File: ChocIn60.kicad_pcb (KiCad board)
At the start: 2 copper layers, 285 x 94.6 mm, 9 parts

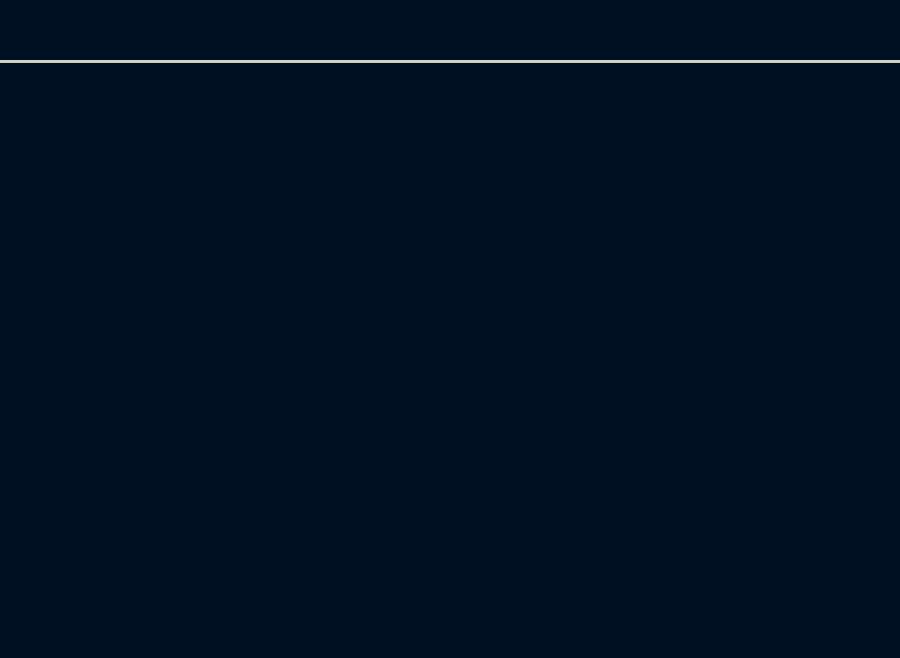
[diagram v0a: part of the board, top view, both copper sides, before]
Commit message: add USB2.0 Type-C Plug.
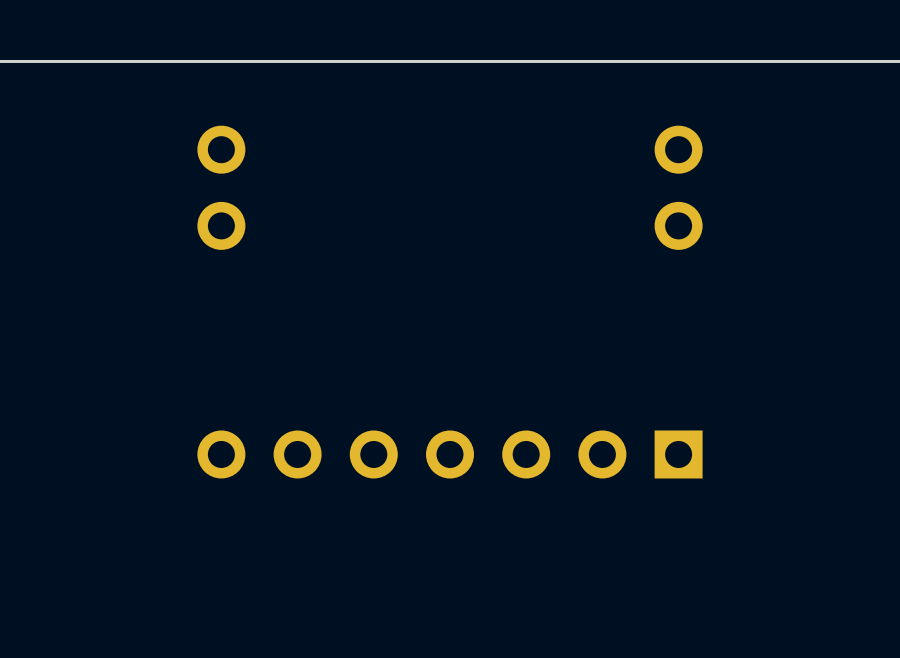
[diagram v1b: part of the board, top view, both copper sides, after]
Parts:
- added P1: USB_C_Plug_USB2.0, Akizuki:AE-USB2.0-TYPE-C, B.Cu at (58.0, 60.0)
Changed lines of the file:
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@@
     (tracks 0)
     (zones 0)
-    (modules 9)
-    (nets 2)
+    (modules 10)
+    (nets 8)
   )
   (page A3)
@@
   (net 0 "")
   (net 1 GND)
+  (net 2 "Net-(P1-PadB5)")
+  (net 3 "Net-(P1-PadA5)")
+  (net 4 "Net-(P1-PadA6)")
+  (net 5 "Net-(P1-PadA7)")
+  (net 6 VCC)
+  (net 7 "Net-(P1-PadS1)")
   (net_class Default "これはデフォルトのネット クラスです。"
     (clearance 0.2)
@@
     (uvia_drill 0.1)
     (add_net GND)
+    (add_net "Net-(P1-PadA5)")
+    (add_net "Net-(P1-PadA6)")
+    (add_net "Net-(P1-PadA7)")
+    (add_net "Net-(P1-PadB5)")
+    (add_net "Net-(P1-PadS1)")
+    (add_net VCC)
+  )
+  (module Akizuki:AE-USB2.0-TYPE-C (layer B.Cu)
+    (at 58 60 180)
+    (descr http://akizukidenshi.com/catalog/g/gK-13080/)
+    (fp_text reference P1 (at 0 -6 180) (layer B.SilkS)
+      (effects (font (size 1 1) (thickness 0.15)) (justify mirror))
+    )
+    (fp_text value USB_C_Plug_USB2.0 (at 0 11 180) (layer B.Fab)
+      (effects (font (size 1 1) (thickness 0.15)) (justify mirror))
+    )
+    (fp_text user GND (at 7.62 0 270 unlocked) (layer B.SilkS)
+      (effects (font (size 1 1) (thickness 0.15)) (justify mirror))
+    )
+    (fp_text user CC2 (at 5.08 0 270 unlocked) (layer B.SilkS)
+      (effects (font (size 1 1) (thickness 0.15)) (justify mirror))
+    )
+    (fp_text user CC1 (at 2.54 0 270 unlocked) (layer B.SilkS)
+      (effects (font (size 1 1) (thickness 0.15)) (justify mirror))
+    )
+    (fp_text user GND (at 0 0 270 unlocked) (layer B.SilkS)
+      (effects (font (size 1 1) (thickness 0.15)) (justify mirror))
+    )
+    (fp_text user D+ (at -2.54 0 270 unlocked) (layer B.SilkS)
+      (effects (font (size 1 1) (thickness 0.15)) (justify mirror))
+    )
+    (fp_text user D- (at -5.08 0 270 unlocked) (layer B.SilkS)
+      (effects (font (size 1 1) (thickness 0.15)) (justify mirror))
+    )
+    (fp_text user VBUS (at -7.62 0 270 unlocked) (layer B.SilkS)
+      (effects (font (size 1 1) (thickness 0.15)) (justify mirror))
+    )
+    (fp_text user AE-USB2.0-TYPE-C (at 0 5) (layer B.SilkS)
+      (effects (font (size 0.75 0.75) (thickness 0.125)) (justify mirror))
+    )
+    (fp_line (start 10 -5) (end 10 10) (layer B.SilkS) (width 0.15))
+    (fp_line (start -10 -5) (end 10 -5) (layer B.SilkS) (width 0.15))
+    (fp_line (start -10 10) (end -10 -5) (layer B.SilkS) (width 0.15))
+    (fp_line (start -10 10) (end 10 10) (layer B.SilkS) (width 0.15))
+    (pad A1 thru_hole circle (at 7.62 -3.1 180) (size 1.6 1.6) (drill 0.9) (layers *.Cu *.Mask)
+      (net 1 GND))
+    (pad B5 thru_hole circle (at 5.08 -3.1 180) (size 1.6 1.6) (drill 0.9) (layers *.Cu *.Mask)
+      (net 2 "Net-(P1-PadB5)"))
+    (pad A5 thru_hole circle (at 2.54 -3.1 180) (size 1.6 1.6) (drill 0.9) (layers *.Cu *.Mask)
+      (net 3 "Net-(P1-PadA5)"))
+    (pad A1 thru_hole circle (at 0 -3.1 180) (size 1.6 1.6) (drill 0.9) (layers *.Cu *.Mask)
+      (net 1 GND))
+    (pad A6 thru_hole circle (at -2.54 -3.1 180) (size 1.6 1.6) (drill 0.9) (layers *.Cu *.Mask)
+      (net 4 "Net-(P1-PadA6)"))
+    (pad A7 thru_hole circle (at -5.08 -3.1 180) (size 1.6 1.6) (drill 0.9) (layers *.Cu *.Mask)
+      (net 5 "Net-(P1-PadA7)"))
+    (pad A4 thru_hole rect (at -7.62 -3.1 90) (size 1.6 1.6) (drill 0.9) (layers *.Cu *.Mask)
+      (net 6 VCC))
+    (pad S1 thru_hole circle (at 7.62 7.06 180) (size 1.6 1.6) (drill 0.9) (layers *.Cu *.Mask)
+      (net 7 "Net-(P1-PadS1)"))
+    (pad S1 thru_hole circle (at 7.62 4.52 180) (size 1.6 1.6) (drill 0.9) (layers *.Cu *.Mask)
+      (net 7 "Net-(P1-PadS1)"))
+    (pad S1 thru_hole circle (at -7.62 4.52 180) (size 1.6 1.6) (drill 0.9) (layers *.Cu *.Mask)
+      (net 7 "Net-(P1-PadS1)"))
+    (pad S1 thru_hole circle (at -7.62 7.06 180) (size 1.6 1.6) (drill 0.9) (layers *.Cu *.Mask)
+      (net 7 "Net-(P1-PadS1)"))
   )
   (module gh60_hole:PKRH (layer F.Cu)

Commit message: マトリクス書いて、基板に配置してみる(WIP)
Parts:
- added D00, D01, D02, D03, D04, D05, D06, D07, D08, D09, D10, D11, D12, D13, D14, D15, D16, D17, D18, D19, D20, D21, D22, D23, D24, D25, D26, D27, D28, D29, D30, D31, D32, D33, D34, D35, D36, D37, D38, D39, D40, D41, D42, D43, D44, D45, D46, D47, D48, D49, D50, D51, D52, D53, D54, D55, D56, D57, D58, D59, D60, D61, D62, D63, D64, D65, D66, D67, D68, D69, D70, D71, D72, D73, D74, D75, D76, D77, D78, D79, D80, D81, D82, D83, D84, D85, D86, D87, D88, D89, D90, D91, D92, D93, D94, D95, D96, D97, D98, D99: D, Diode_SMD:D_SOD-123, F.Cu at (42.8, 219.1)
- added SW00: SW_Push, Keebio-Parts_mod:Kailh-PG1350-1u-no-LED, F.Cu at (266.4, 105.1)
- added SW01: SW_Push, Keebio-Parts_mod:Kailh-PG1350-1u-no-LED, F.Cu at (81.6, 105.1)
- added SW02: SW_Push, Keebio-Parts_mod:Kailh-PG1350-1u-no-LED, F.Cu at (64.8, 105.1)
- added SW03: SW_Push, Keebio-Parts_mod:Kailh-PG1350-1u-no-LED, F.Cu at (48.0, 105.1)
- added SW04: SW_Push, Keebio-Parts_mod:Kailh-PG1350-1u-no-LED, F.Cu at (81.6, 120.9)
- added SW05: SW_Push, Keebio-Parts_mod:Kailh-PG1350-1u-no-LED, F.Cu at (64.8, 120.9)
- added SW06: SW_Push, Keebio-Parts_mod:Kailh-PG1350-1u-no-LED, F.Cu at (48.0, 120.9)
- added SW07: SW_Push, Keebio-Parts_mod:Kailh-PG1350-1u-no-LED, F.Cu at (316.8, 105.1)
- added SW08: SW_Push, Keebio-Parts_mod:Kailh-PG1350-1u-no-LED, F.Cu at (300.0, 105.1)
- added SW09: SW_Push, Keebio-Parts_mod:Kailh-PG1350-1u-no-LED, F.Cu at (283.2, 105.1)
- added SW10: SW_Push, Keebio-Parts_mod:Kailh-PG1350-1u-no-LED, F.Cu at (249.6, 57.7)
- added SW11: SW_Push, Keebio-Parts_mod:Kailh-PG1350-1u-no-LED, F.Cu at (98.4, 57.7)
- added SW12: SW_Push, Keebio-Parts_mod:Kailh-PG1350-1u-no-LED, F.Cu at (115.2, 57.7)
- added SW13: SW_Push, Keebio-Parts_mod:Kailh-PG1350-1u-no-LED, F.Cu at (132.0, 57.7)
- added SW14: SW_Push, Keebio-Parts_mod:Kailh-PG1350-1u-no-LED, F.Cu at (148.8, 57.7)
- added SW15: SW_Push, Keebio-Parts_mod:Kailh-PG1350-1u-no-LED, F.Cu at (165.6, 57.7)
- added SW16: SW_Push, Keebio-Parts_mod:Kailh-PG1350-1u-no-LED, F.Cu at (182.4, 57.7)
- added SW17: SW_Push, Keebio-Parts_mod:Kailh-PG1350-1u-no-LED, F.Cu at (199.2, 57.7)
- added SW18: SW_Push, Keebio-Parts_mod:Kailh-PG1350-1u-no-LED, F.Cu at (216.0, 57.7)
- added SW19: SW_Push, Keebio-Parts_mod:Kailh-PG1350-1u-no-LED, F.Cu at (232.8, 57.7)
- added SW20: SW_Push, Keebio-Parts_mod:Kailh-PG1350-1u-no-LED, F.Cu at (249.6, 73.5)
- added SW21: SW_Push, Keebio-Parts_mod:Kailh-PG1350-1u-no-LED, F.Cu at (98.4, 73.5)
- added SW22: SW_Push, Keebio-Parts_mod:Kailh-PG1350-1u-no-LED, F.Cu at (115.2, 73.5)
- added SW23: SW_Push, Keebio-Parts_mod:Kailh-PG1350-1u-no-LED, F.Cu at (132.0, 73.5)
- added SW24: SW_Push, Keebio-Parts_mod:Kailh-PG1350-1u-no-LED, F.Cu at (148.8, 73.5)
- added SW25: SW_Push, Keebio-Parts_mod:Kailh-PG1350-1u-no-LED, F.Cu at (165.6, 73.5)
- added SW26: SW_Push, Keebio-Parts_mod:Kailh-PG1350-1u-no-LED, F.Cu at (182.4, 73.5)
- added SW27: SW_Push, Keebio-Parts_mod:Kailh-PG1350-1u-no-LED, F.Cu at (199.2, 73.5)
- added SW28: SW_Push, Keebio-Parts_mod:Kailh-PG1350-1u-no-LED, F.Cu at (216.0, 73.5)
- added SW29: SW_Push, Keebio-Parts_mod:Kailh-PG1350-1u-no-LED, F.Cu at (232.8, 73.5)
- added SW30: SW_Push, Keebio-Parts_mod:Kailh-PG1350-1u-no-LED, F.Cu at (249.6, 89.3)
- added SW31: SW_Push, Keebio-Parts_mod:Kailh-PG1350-1u-no-LED, F.Cu at (98.4, 89.3)
- added SW32: SW_Push, Keebio-Parts_mod:Kailh-PG1350-1u-no-LED, F.Cu at (115.2, 89.3)
- added SW33: SW_Push, Keebio-Parts_mod:Kailh-PG1350-1u-no-LED, F.Cu at (132.0, 89.3)
- added SW34: SW_Push, Keebio-Parts_mod:Kailh-PG1350-1u-no-LED, F.Cu at (148.8, 89.3)
- added SW35: SW_Push, Keebio-Parts_mod:Kailh-PG1350-1u-no-LED, F.Cu at (165.6, 89.3)
- added SW36: SW_Push, Keebio-Parts_mod:Kailh-PG1350-1u-no-LED, F.Cu at (182.4, 89.3)
- added SW37: SW_Push, Keebio-Parts_mod:Kailh-PG1350-1u-no-LED, F.Cu at (199.2, 89.3)
- added SW38: SW_Push, Keebio-Parts_mod:Kailh-PG1350-1u-no-LED, F.Cu at (216.0, 89.3)
- added SW39: SW_Push, Keebio-Parts_mod:Kailh-PG1350-1u-no-LED, F.Cu at (232.8, 89.3)
- added SW40: SW_Push, Keebio-Parts_mod:Kailh-PG1350-1u-no-LED, F.Cu at (249.6, 105.1)
- added SW41: SW_Push, Keebio-Parts_mod:Kailh-PG1350-1u-no-LED, F.Cu at (98.4, 105.1)
- added SW42: SW_Push, Keebio-Parts_mod:Kailh-PG1350-1u-no-LED, F.Cu at (115.2, 105.1)
- added SW43: SW_Push, Keebio-Parts_mod:Kailh-PG1350-1u-no-LED, F.Cu at (132.0, 105.1)
- added SW44: SW_Push, Keebio-Parts_mod:Kailh-PG1350-1u-no-LED, F.Cu at (148.8, 105.1)
- added SW45: SW_Push, Keebio-Parts_mod:Kailh-PG1350-1u-no-LED, F.Cu at (165.6, 105.1)
- added SW46: SW_Push, Keebio-Parts_mod:Kailh-PG1350-1u-no-LED, F.Cu at (182.4, 105.1)
- added SW47: SW_Push, Keebio-Parts_mod:Kailh-PG1350-1u-no-LED, F.Cu at (199.2, 105.1)
- added SW48: SW_Push, Keebio-Parts_mod:Kailh-PG1350-1u-no-LED, F.Cu at (216.0, 105.1)
- added SW49: SW_Push, Keebio-Parts_mod:Kailh-PG1350-1u-no-LED, F.Cu at (232.8, 105.1)
- added SW50: SW_Push, Keebio-Parts_mod:Kailh-PG1350-1u-no-LED, F.Cu at (266.4, 120.9)
- added SW51: SW_Push, Keebio-Parts_mod:Kailh-PG1350-1u-no-LED, F.Cu at (98.4, 120.9)
- added SW52: SW_Push, Keebio-Parts_mod:Kailh-PG1350-1u-no-LED, F.Cu at (115.2, 120.9)
- added SW53: SW_Push, Keebio-Parts_mod:Kailh-PG1350-1u-no-LED, F.Cu at (132.0, 120.9)
- added SW54: SW_Push, Keebio-Parts_mod:Kailh-PG1350-1u-no-LED, F.Cu at (148.8, 120.9)
- added SW55: SW_Push, Keebio-Parts_mod:Kailh-PG1350-1u-no-LED, F.Cu at (165.6, 120.9)
- added SW56: SW_Push, Keebio-Parts_mod:Kailh-PG1350-1u-no-LED, F.Cu at (182.4, 120.9)
- added SW57: SW_Push, Keebio-Parts_mod:Kailh-PG1350-1u-no-LED, F.Cu at (199.2, 120.9)
- added SW58: SW_Push, Keebio-Parts_mod:Kailh-PG1350-1u-no-LED, F.Cu at (216.0, 120.9)
- added SW59: SW_Push, Keebio-Parts_mod:Kailh-PG1350-1u-no-LED, F.Cu at (232.8, 120.9)
- added SW60: SW_Push, Keebio-Parts_mod:Kailh-PG1350-1u-no-LED, F.Cu at (249.6, 136.7)
- added SW61: SW_Push, Keebio-Parts_mod:Kailh-PG1350-1u-no-LED, F.Cu at (98.4, 136.7)
- added SW62: SW_Push, Keebio-Parts_mod:Kailh-PG1350-1u-no-LED, F.Cu at (115.2, 136.7)
- added SW63: SW_Push, Keebio-Parts_mod:Kailh-PG1350-1u-no-LED, F.Cu at (132.0, 136.7)
- added SW64: SW_Push, Keebio-Parts_mod:Kailh-PG1350-1u-no-LED, F.Cu at (148.8, 136.7)
- added SW65: SW_Push, Keebio-Parts_mod:Kailh-PG1350-1u-no-LED, F.Cu at (165.6, 136.7)
- added SW66: SW_Push, Keebio-Parts_mod:Kailh-PG1350-1u-no-LED, F.Cu at (182.4, 136.7)
- added SW67: SW_Push, Keebio-Parts_mod:Kailh-PG1350-1u-no-LED, F.Cu at (199.2, 136.7)
- added SW68: SW_Push, Keebio-Parts_mod:Kailh-PG1350-1u-no-LED, F.Cu at (216.0, 136.7)
- added SW69: SW_Push, Keebio-Parts_mod:Kailh-PG1350-1u-no-LED, F.Cu at (249.6, 120.9)
- added SW70: SW_Push, Keebio-Parts_mod:Kailh-PG1350-1u-no-LED, F.Cu at (266.4, 57.7)
- added SW71: SW_Push, Keebio-Parts_mod:Kailh-PG1350-1u-no-LED, F.Cu at (81.6, 57.7)
- added SW72: SW_Push, Keebio-Parts_mod:Kailh-PG1350-1u-no-LED, F.Cu at (64.8, 57.7)
- added SW73: SW_Push, Keebio-Parts_mod:Kailh-PG1350-1u-no-LED, F.Cu at (48.0, 57.7)
- added SW74: SW_Push, Keebio-Parts_mod:Kailh-PG1350-1u-no-LED, F.Cu at (266.4, 136.7)
- added SW75: SW_Push, Keebio-Parts_mod:Kailh-PG1350-1u-no-LED, F.Cu at (283.2, 136.7)
- added SW76: SW_Push, Keebio-Parts_mod:Kailh-PG1350-1u-no-LED, F.Cu at (316.8, 136.7)
- added SW77: SW_Push, Keebio-Parts_mod:Kailh-PG1350-1u-no-LED, F.Cu at (316.8, 57.7)
- added SW78: SW_Push, Keebio-Parts_mod:Kailh-PG1350-1u-no-LED, F.Cu at (300.0, 57.7)
- added SW79: SW_Push, Keebio-Parts_mod:Kailh-PG1350-1u-no-LED, F.Cu at (283.2, 57.7)
- added SW80: SW_Push, Keebio-Parts_mod:Kailh-PG1350-1u-no-LED, F.Cu at (266.4, 73.5)
- added SW81: SW_Push, Keebio-Parts_mod:Kailh-PG1350-1u-no-LED, F.Cu at (81.6, 73.5)
- added SW82: SW_Push, Keebio-Parts_mod:Kailh-PG1350-1u-no-LED, F.Cu at (64.8, 73.5)
- added SW83: SW_Push, Keebio-Parts_mod:Kailh-PG1350-1u-no-LED, F.Cu at (48.0, 73.5)
- added SW84: SW_Push, Keebio-Parts_mod:Kailh-PG1350-1u-no-LED, F.Cu at (283.2, 120.9)
- added SW85: SW_Push, Keebio-Parts_mod:Kailh-PG1350-1u-no-LED, F.Cu at (300.0, 120.9)
- added SW86: SW_Push, Keebio-Parts_mod:Kailh-PG1350-1u-no-LED, F.Cu at (316.8, 120.9)
- added SW87: SW_Push, Keebio-Parts_mod:Kailh-PG1350-1u-no-LED, F.Cu at (316.8, 73.5)
- added SW88: SW_Push, Keebio-Parts_mod:Kailh-PG1350-1u-no-LED, B.Cu at (300.0, 73.5)
- added SW89: SW_Push, Keebio-Parts_mod:Kailh-PG1350-1u-no-LED, F.Cu at (283.2, 73.5)
- added SW90: SW_Push, Keebio-Parts_mod:Kailh-PG1350-1u-no-LED, F.Cu at (266.4, 89.3)
- added SW91: SW_Push, Keebio-Parts_mod:Kailh-PG1350-1u-no-LED, F.Cu at (81.6, 89.3)
- added SW92: SW_Push, Keebio-Parts_mod:Kailh-PG1350-1u-no-LED, F.Cu at (64.8, 89.3)
- added SW93: SW_Push, Keebio-Parts_mod:Kailh-PG1350-1u-no-LED, F.Cu at (48.0, 89.3)
- added SW94: SW_Push, Keebio-Parts_mod:Kailh-PG1350-1u-no-LED, F.Cu at (81.6, 136.7)
- added SW95: SW_Push, Keebio-Parts_mod:Kailh-PG1350-1u-no-LED, F.Cu at (64.8, 136.7)
- added SW96: SW_Push, Keebio-Parts_mod:Kailh-PG1350-1u-no-LED, F.Cu at (48.0, 136.7)
- added SW97: SW_Push, Keebio-Parts_mod:Kailh-PG1350-1u-no-LED, F.Cu at (316.8, 89.3)
- added SW98: SW_Push, Keebio-Parts_mod:Kailh-PG1350-1u-no-LED, F.Cu at (300.0, 89.3)
- added SW99: SW_Push, Keebio-Parts_mod:Kailh-PG1350-1u-no-LED, F.Cu at (283.2, 89.3)

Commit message: wip
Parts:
- removed P1: USB_C_Plug_USB2.0, Akizuki:AE-USB2.0-TYPE-C
- added J1: USB_B_Micro, Connector_USB:USB_Micro-B_Amphenol_10103594-0001LF_Horizontal, B.Cu at (58.2, 52.8)
- renumbered D00 to D0, D01 to D1, D02 to D2, D03 to D3, D04 to D4, D05 to D5, D06 to D6, D07 to D7, D08 to D8, D09 to D9, SW00 to SW0, SW01 to SW1, SW02 to SW2, SW03 to SW3, SW04 to SW4, SW05 to SW5, SW06 to SW6, SW07 to SW7, SW08 to SW8, SW09 to SW9

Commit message: [WIP] キー数を減らす
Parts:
- removed D0, D2, D35, D36, D5, D70, D72, D80, D82, D90, D92, D95: D, Diode_SMD:D_SOD-123
- removed SW0, SW2, SW35, SW36, SW5, SW70, SW72, SW80, SW82, SW90, SW92, SW95: SW_Push, Keebio-Parts_mod:Kailh-PG1350-1u-no-LED

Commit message: キー数を減らした
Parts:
- SW88: moved to F.Cu
- moved D1 194.8 mm to (112.3, 37.1)
- moved D10 194.8 mm to (112.3, 37.1)
- moved D11 194.8 mm to (112.3, 37.1)
- moved D12 194.8 mm to (112.3, 37.1)
- moved D13 194.8 mm to (112.3, 37.1)
- moved D14 194.8 mm to (112.3, 37.1)
- moved D15 194.8 mm to (112.3, 37.1)
- moved D16 194.8 mm to (112.3, 37.1)
- moved D17 194.8 mm to (112.3, 37.1)
- moved D18 194.8 mm to (112.3, 37.1)
- moved D19 194.8 mm to (112.3, 37.1)
- moved D20 194.8 mm to (112.3, 37.1)
- moved D21 194.8 mm to (112.3, 37.1)
- moved D22 194.8 mm to (112.3, 37.1)
- moved D23 194.8 mm to (112.3, 37.1)
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
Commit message: リセットスイッチ配置
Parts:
- added SW_R0: SW_Push, Akizuki:SW_Push_ALPS_SKRPACE010, B.Cu at (69.2, 98.2)
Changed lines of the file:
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@@
     (tracks 0)
     (zones 0)
-    (modules 186)
-    (nets 115)
+    (modules 187)
+    (nets 116)
   )
   (page A3)
@@
     (47 F.CrtYd user)
     (48 B.Fab user)
-    (49 F.Fab user)
+    (49 F.Fab user hide)
   )
   (setup
@@
     (solder_mask_min_width 0.25)
     (aux_axis_origin 40 50)
-    (visible_elements 7FFFF7FF)
+    (visible_elements 7FFFFFFF)
     (pcbplotparams
       (layerselection 0x010fc_ffffffff)
@@
   (net 113 "Net-(J1-Pad3)")
   (net 114 "Net-(J1-Pad2)")
+  (net 115 "Net-(SW_R0-Pad2)")
   (net_class Default "これはデフォルトのネット クラスです。"
     (clearance 0.2)
@@
     (add_net "Net-(J1-Pad4)")
     (add_net "Net-(J1-Pad6)")
+    (add_net "Net-(SW_R0-Pad2)")
     (add_net VCC)
   )
+  (module Akizuki:SW_Push_ALPS_SKRPACE010 (layer B.Cu)
+    (at 69.241 98.218)
+    (descr http://akizukidenshi.com/catalog/g/gP-06185/)
+    (attr smd)
+    (fp_text reference SW_R0 (at 0 -2.5) (layer B.SilkS)
+      (effects (font (size 1 1) (thickness 0.15)) (justify mirror))
+    )
+    (fp_text value SW_Push (at 0 2.5) (layer B.Fab)
+      (effects (font (size 1 1) (thickness 0.15)) (justify mirror))
+    )
+    (fp_line (start -0.4 -1.1) (end 0.4 -1.1) (layer B.SilkS) (width 0.12))
+    (fp_line (start -0.4 1.1) (end 0.4 1.1) (layer B.SilkS) (width 0.12))
+    (fp_arc (start 0.4 0) (end 0.4 -1.1) (angle 180) (layer B.SilkS) (width 0.12))
+    (fp_line (start -2.1 1.55) (end 2.1 1.55) (layer B.SilkS) (width 0.12))
+    (fp_line (start 2.1 1.55) (end 2.1 -1.65) (layer B.SilkS) (width 0.12))
+    (fp_line (start 2.1 -1.65) (end -2.1 -1.65) (layer B.SilkS) (width 0.12))
+    (fp_line (start -2.1 -1.65) (end -2.1 1.55) (layer B.SilkS) (width 0.12))
+    (fp_arc (start -0.4 0) (end -0.4 1.1) (angle 180) (layer B.SilkS) (width 0.12))
+    (pad 2 smd rect (at 2.05 -1.05) (size 2 1) (layers B.Cu B.Paste B.Mask)
+      (net 115 "Net-(SW_R0-Pad2)"))
+    (pad 1 smd rect (at 2.1 1) (size 2 1) (layers B.Cu B.Paste B.Mask)
+      (net 1 GND))
+    (pad 1 smd rect (at -2 1) (size 2 1) (layers B.Cu B.Paste B.Mask)
+      (net 1 GND))
+    (pad 2 smd rect (at -2 -1.1) (size 2 1) (layers B.Cu B.Paste B.Mask)
+      (net 115 "Net-(SW_R0-Pad2)"))
+  )
   (module Keebio-Parts_mod:Kailh-PG1350-1u-no-LED (layer F.Cu)
     (at 266.15 89.49)
@@
     )
   )
+  (dimension 27.9 (width 0.3048) (layer Cmts.User)
+    (gr_text "27.900 mm" (at 25.8844 63.95 90) (layer Cmts.User)
+      (effects (font (size 2.032 1.524) (thickness 0.3048)))
+    )
+    (feature1 (pts (xy 65.22 50) (xy 24.2588 50)))
+    (feature2 (pts (xy 65.22 77.9) (xy 24.2588 77.9)))
+    (crossbar (pts (xy 27.51 77.9) (xy 27.51 50)))
+    (arrow1a (pts (xy 27.51 50) (xy 28.096421 51.126504)))
+    (arrow1b (pts (xy 27.51 50) (xy 26.923579 51.126504)))
+    (arrow2a (pts (xy 27.51 77.9) (xy 28.096421 76.773496)))
+    (arrow2b (pts (xy 27.51 77.9) (xy 26.923579 76.773496)))
+  )
   (target plus (at 40 50) (size 5) (width 0.05) (layer Edge.Cuts))
   (gr_text + (at 50.227 104.395) (layer B.SilkS)
@@
   (gr_line (start 334 124.8) (end 334 126.8) (angle 90) (layer Eco1.User) (width 0.381))
   (gr_line (start 334 141.4) (end 334 143.4) (angle 90) (layer Eco1.User) (width 0.381))
-  (dimension 27.9 (width 0.3048) (layer Cmts.User)
-    (gr_text "27.900 mm" (at 25.8844 63.95 90) (layer Cmts.User)
-      (effects (font (size 2.032 1.524) (thickness 0.3048)))
-    )
-    (feature1 (pts (xy 65.22 50) (xy 24.2588 50)))
-    (feature2 (pts (xy 65.22 77.9) (xy 24.2588 77.9)))
-    (crossbar (pts (xy 27.51 77.9) (xy 27.51 50)))
-    (arrow1a (pts (xy 27.51 50) (xy 28.096421 51.126504)))
-    (arrow1b (pts (xy 27.51 50) (xy 26.923579 51.126504)))
-    (arrow2a (pts (xy 27.51 77.9) (xy 28.096421 76.773496)))
-    (arrow2b (pts (xy 27.51 77.9) (xy 26.923579 76.773496)))
-  )
   (dimension 24.95 (width 0.3048) (layer Cmts.User)
     (gr_text "24.950 mm" (at 312.525 23.054401) (layer Cmts.User)

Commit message: レイアウト調整
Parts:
- removed D62, D69: D, Diode_SMD:D_SOD-123
- removed SW62, SW69: SW_Push, Keebio-Parts_mod:Kailh-PG1350-1u-no-LED
- added D70: D, Diode_SMD:D_SOD-123, F.Cu at (284.2, 29.6)
- added D72: D, Diode_SMD:D_SOD-123, F.Cu at (23.8, 21.4)
- added SW70: SW_Push, Keebio-Parts_mod:Kailh-PG1350-1u-no-LED, F.Cu at (266.1, 58.5)
- added SW72: SW_Push, Keebio-Parts_mod:Kailh-PG1350-1u-no-LED, F.Cu at (65.2, 58.5)
- moved SW78 16.8 mm to (299.6, 58.5)
- moved SW79 16.8 mm to (282.9, 58.5)
- moved SW3 8.39 mm to (56.8, 105.0)
- moved SW6 8.39 mm to (56.8, 120.5)
- moved SW7 8.39 mm to (308.0, 105.0)
- moved SW86 8.39 mm to (308.0, 120.5)

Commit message: ネットクラス VCC の配線の太さを指定
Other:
- net class VCC added: clearance 0.2, trace_width 0.5, via_dia 0.8, via_drill 0.4
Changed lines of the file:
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@@
     (add_net "Net-(J1-Pad6)")
     (add_net "Net-(SW_R0-Pad2)")
+  )
+  (net_class VCC ""
+    (clearance 0.2)
+    (trace_width 0.5)
+    (via_dia 0.8)
+    (via_drill 0.4)
+    (uvia_dia 0.3)
+    (uvia_drill 0.1)
     (add_net VCC)
   )
